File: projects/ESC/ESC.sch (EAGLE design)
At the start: 93 parts, among them J1 1755529, J2 1755529, J3 1755529, J4 1755529, U1 STM32F405RGT6, U10 CSD88584Q5DCT, U11 CSD88584Q5DCT, U12 CSD88584Q5DCT, U13 CSD88584Q5DCT, U14 SN74CBTLV3257PWR, U15 CSD88584Q5DCT, U16 CSD88584Q5DCT, U17 CSD88584Q5DCT, U2 CSD88584Q5DCT, U3 CSD88584Q5DCT, U4 CSD88584Q5DCT, U8 CSD88584Q5DCT, U9 CSD88584Q5DCT, Y1 ECS-80-S-4X

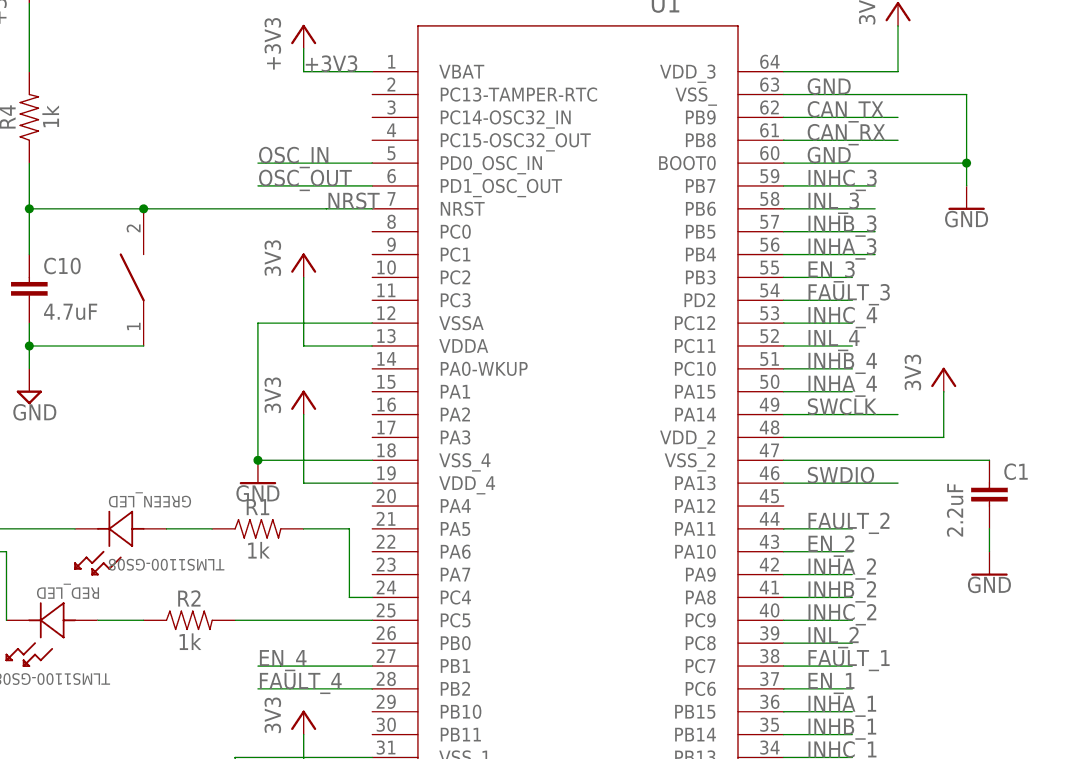
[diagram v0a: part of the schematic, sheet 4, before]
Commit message: All DRVs connected to STM
now for the fun part...
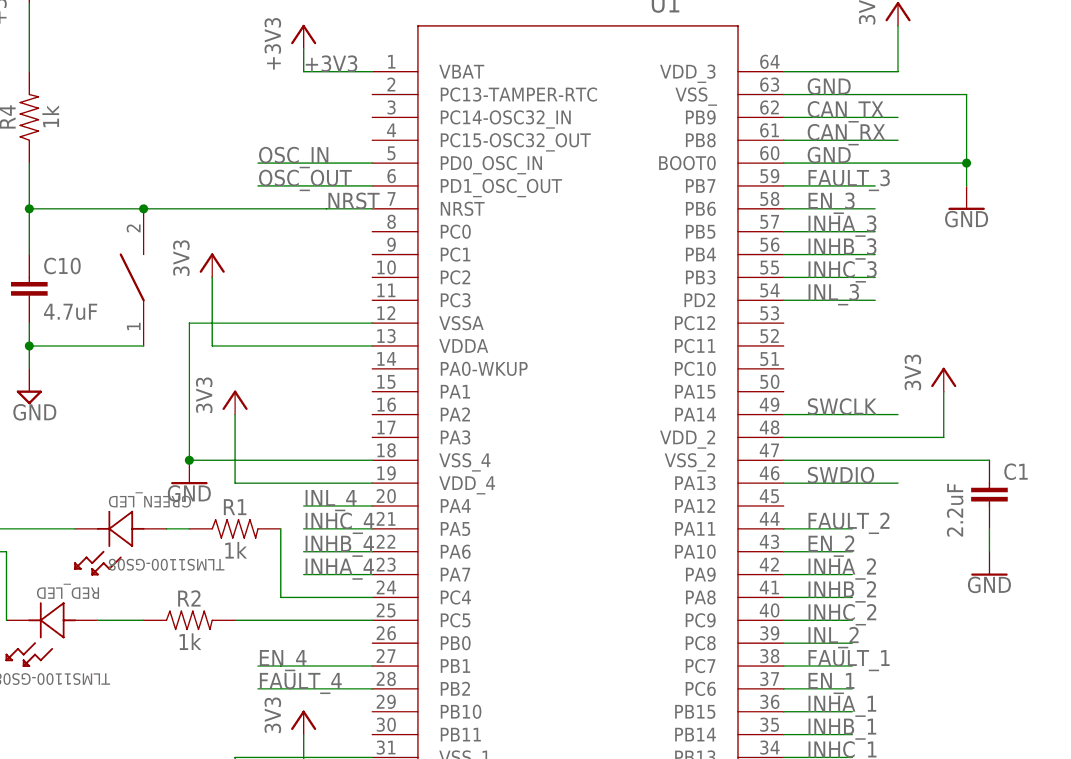
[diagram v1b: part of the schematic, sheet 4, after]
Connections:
- net EN_3: now also U1.PB6; no longer U1.PB3
- net FAULT_3: now also U1.PB7; no longer U1.PD2
- net INHA_3: now also U1.PB5; no longer U1.PB4
- net INHA_4: now also U1.PA7; no longer U1.PA15
- net INHB_3: now also U1.PB4; no longer U1.PB5
- net INHB_4: now also U1.PA6; no longer U1.PC10
- net INHC_3: now also U1.PB3; no longer U1.PB7
- net INHC_4: now also U1.PA5; no longer U1.PC12
- net INL_3: now also U1.PD2; no longer U1.PB6
- net INL_4: now also U1.PA4; no longer U1.PC11
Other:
- moved on the sheet: R1
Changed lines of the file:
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@@
 <attribute name="VALUE" x="91.1606" y="113.2586" size="2.0828" layer="96" ratio="6" rot="SR0"/>
 </instance>
-<instance part="R1" gate="G$1" x="63.5" y="53.34" smashed="yes">
-<attribute name="NAME" x="63.5" y="54.864" size="1.778" layer="95" font="vector" align="bottom-center"/>
-<attribute name="VALUE" x="63.5" y="51.816" size="1.778" layer="96" font="vector" align="top-center"/>
+<instance part="R1" gate="G$1" x="60.96" y="53.34" smashed="yes">
+<attribute name="NAME" x="60.96" y="54.864" size="1.778" layer="95" font="vector" align="bottom-center"/>
+<attribute name="VALUE" x="60.96" y="51.816" size="1.778" layer="96" font="vector" align="top-center"/>
 </instance>
 <instance part="R2" gate="G$1" x="55.88" y="43.18" smashed="yes">
@@
 <attribute name="VALUE" x="142.24" y="88.646" size="1.778" layer="96" align="top-center"/>
 </instance>
-<instance part="GND24" gate="1" x="63.5" y="58.42" smashed="yes">
-<attribute name="VALUE" x="63.5" y="58.166" size="1.778" layer="96" align="top-center"/>
-</instance>
-<instance part="3V1" gate="VCC" x="68.58" y="83.82" smashed="yes">
-<attribute name="VALUE" x="66.04" y="81.28" size="1.778" layer="96" rot="R90"/>
+<instance part="GND24" gate="1" x="55.88" y="58.42" smashed="yes">
+<attribute name="VALUE" x="55.88" y="58.166" size="1.778" layer="96" align="top-center"/>
+</instance>
+<instance part="3V1" gate="VCC" x="58.42" y="83.82" smashed="yes">
+<attribute name="VALUE" x="55.88" y="81.28" size="1.778" layer="96" rot="R90"/>
 </instance>
 <instance part="C10" gate="G$1" x="38.1" y="78.74" smashed="yes">
@@
 <attribute name="VALUE" x="137.16" y="68.58" size="1.778" layer="96" rot="R90"/>
 </instance>
-<instance part="3V6" gate="VCC" x="68.58" y="68.58" smashed="yes">
-<attribute name="VALUE" x="66.04" y="66.04" size="1.778" layer="96" rot="R90"/>
+<instance part="3V6" gate="VCC" x="60.96" y="68.58" smashed="yes">
+<attribute name="VALUE" x="58.42" y="66.04" size="1.778" layer="96" rot="R90"/>
 </instance>
 <instance part="3V7" gate="VCC" x="68.58" y="33.02" smashed="yes">
@@
 <segment>
 <pinref part="U1" gate="A" pin="PC4"/>
-<wire x1="76.2" y1="45.72" x2="73.66" y2="45.72" width="0.1524" layer="91"/>
 <pinref part="R1" gate="G$1" pin="2"/>
-<wire x1="68.58" y1="53.34" x2="73.66" y2="53.34" width="0.1524" layer="91"/>
-<wire x1="73.66" y1="53.34" x2="73.66" y2="45.72" width="0.1524" layer="91"/>
+<wire x1="66.04" y1="53.34" x2="66.04" y2="45.72" width="0.1524" layer="91"/>
+<wire x1="66.04" y1="45.72" x2="76.2" y2="45.72" width="0.1524" layer="91"/>
 </segment>
 </net>
@@
 <pinref part="R1" gate="G$1" pin="1"/>
 <pinref part="GREEN_LED" gate="A" pin="2"/>
-<wire x1="53.34" y1="53.34" x2="58.42" y2="53.34" width="0.1524" layer="91"/>
+<wire x1="53.34" y1="53.34" x2="55.88" y2="53.34" width="0.1524" layer="91"/>
 </segment>
 </net>
@@
 <pinref part="U1" gate="A" pin="VSSA"/>
 <pinref part="GND24" gate="1" pin="GND"/>
-<wire x1="76.2" y1="76.2" x2="63.5" y2="76.2" width="0.1524" layer="91"/>
-<wire x1="63.5" y1="76.2" x2="63.5" y2="60.96" width="0.1524" layer="91"/>
+<wire x1="76.2" y1="76.2" x2="55.88" y2="76.2" width="0.1524" layer="91"/>
+<wire x1="55.88" y1="76.2" x2="55.88" y2="60.96" width="0.1524" layer="91"/>
 <pinref part="U1" gate="A" pin="VSS_4"/>
-<wire x1="76.2" y1="60.96" x2="63.5" y2="60.96" width="0.1524" layer="91"/>
-<junction x="63.5" y="60.96"/>
+<wire x1="76.2" y1="60.96" x2="55.88" y2="60.96" width="0.1524" layer="91"/>
+<junction x="55.88" y="60.96"/>
 </segment>
 <segment>
@@
 </segment>
 </net>
-<net name="FAULT_3" class="0">
-<segment>
-<wire x1="121.92" y1="78.74" x2="129.54" y2="78.74" width="0.1524" layer="91"/>
-<pinref part="U1" gate="A" pin="PD2"/>
-<label x="124.46" y="78.74" size="1.778" layer="95"/>
-</segment>
-</net>
-<net name="INHA_4" class="0">
-<segment>
-<pinref part="U1" gate="A" pin="PA15"/>
-<wire x1="121.92" y1="68.58" x2="129.54" y2="68.58" width="0.1524" layer="91"/>
-<label x="124.46" y="68.58" size="1.778" layer="95"/>
-</segment>
-</net>
-<net name="INHB_4" class="0">
-<segment>
-<pinref part="U1" gate="A" pin="PC10"/>
-<wire x1="121.92" y1="71.12" x2="129.54" y2="71.12" width="0.1524" layer="91"/>
-<label x="124.46" y="71.12" size="1.778" layer="95"/>
-</segment>
-</net>
-<net name="INHC_4" class="0">
-<segment>
-<wire x1="121.92" y1="76.2" x2="129.54" y2="76.2" width="0.1524" layer="91"/>
-<pinref part="U1" gate="A" pin="PC12"/>
-<label x="124.46" y="76.2" size="1.778" layer="95"/>
-</segment>
-</net>
-<net name="INL_4" class="0">
-<segment>
-<wire x1="121.92" y1="73.66" x2="129.54" y2="73.66" width="0.1524" layer="91"/>
-<pinref part="U1" gate="A" pin="PC11"/>
-<label x="124.46" y="73.66" size="1.778" layer="95"/>
-</segment>
-</net>
 <net name="EN_4" class="0">
 <segment>
@@
 <pinref part="U1" gate="A" pin="VDDA"/>
 <pinref part="3V1" gate="VCC" pin="VCC"/>
-<wire x1="76.2" y1="73.66" x2="68.58" y2="73.66" width="0.1524" layer="91"/>
-<wire x1="68.58" y1="73.66" x2="68.58" y2="81.28" width="0.1524" layer="91"/>
+<wire x1="76.2" y1="73.66" x2="58.42" y2="73.66" width="0.1524" layer="91"/>
+<wire x1="58.42" y1="73.66" x2="58.42" y2="81.28" width="0.1524" layer="91"/>
 </segment>
 <segment>
@@
 <segment>
 <pinref part="U1" gate="A" pin="VDD_4"/>
-<wire x1="76.2" y1="58.42" x2="68.58" y2="58.42" width="0.1524" layer="91"/>
+<wire x1="76.2" y1="58.42" x2="60.96" y2="58.42" width="0.1524" layer="91"/>
 <pinref part="3V6" gate="VCC" pin="VCC"/>
-<wire x1="68.58" y1="58.42" x2="68.58" y2="66.04" width="0.1524" layer="91"/>
+<wire x1="60.96" y1="58.42" x2="60.96" y2="66.04" width="0.1524" layer="91"/>
 </segment>
 </net>
@@
 </segment>
 </net>
-<net name="INHC_3" class="0">
+<net name="INL_4" class="0">
+<segment>
+<pinref part="U1" gate="A" pin="PA4"/>
+<wire x1="76.2" y1="55.88" x2="68.58" y2="55.88" width="0.1524" layer="91"/>
+<label x="68.58" y="55.88" size="1.778" layer="95"/>
+</segment>
+</net>
+<net name="INHC_4" class="0">
+<segment>
+<pinref part="U1" gate="A" pin="PA5"/>
+<wire x1="76.2" y1="53.34" x2="68.58" y2="53.34" width="0.1524" layer="91"/>
+<label x="68.58" y="53.34" size="1.778" layer="95"/>
+</segment>
+</net>
+<net name="INHB_4" class="0">
+<segment>
+<pinref part="U1" gate="A" pin="PA6"/>
+<wire x1="76.2" y1="50.8" x2="68.58" y2="50.8" width="0.1524" layer="91"/>
+<label x="68.58" y="50.8" size="1.778" layer="95"/>
+</segment>
+</net>
+<net name="INHA_4" class="0">
+<segment>
+<pinref part="U1" gate="A" pin="PA7"/>
+<wire x1="76.2" y1="48.26" x2="68.58" y2="48.26" width="0.1524" layer="91"/>
+<label x="68.58" y="48.26" size="1.778" layer="95"/>
+</segment>
+</net>
+<net name="FAULT_3" class="0">
 <segment>
 <pinref part="U1" gate="A" pin="PB7"/>
@@
 <net name="EN_3" class="0">
 <segment>
-<wire x1="121.92" y1="81.28" x2="129.54" y2="81.28" width="0.1524" layer="91"/>
-<pinref part="U1" gate="A" pin="PB3"/>
-<label x="124.46" y="81.28" size="1.778" layer="95"/>
+<pinref part="U1" gate="A" pin="PB6"/>
+<wire x1="121.92" y1="88.9" x2="132.08" y2="88.9" width="0.1524" layer="91"/>
+<label x="124.46" y="88.9" size="1.778" layer="95"/>
 </segment>
 </net>
 <net name="INHA_3" class="0">
+<segment>
+<pinref part="U1" gate="A" pin="PB5"/>
+<wire x1="121.92" y1="86.36" x2="132.08" y2="86.36" width="0.1524" layer="91"/>
+<label x="124.46" y="86.36" size="1.778" layer="95"/>
+</segment>
+</net>
+<net name="INHB_3" class="0">
 <segment>
 <pinref part="U1" gate="A" pin="PB4"/>
@@
 </segment>
 </net>
-<net name="INHB_3" class="0">
-<segment>
-<pinref part="U1" gate="A" pin="PB5"/>
-<wire x1="121.92" y1="86.36" x2="132.08" y2="86.36" width="0.1524" layer="91"/>
-<label x="124.46" y="86.36" size="1.778" layer="95"/>
+<net name="INHC_3" class="0">
+<segment>
+<pinref part="U1" gate="A" pin="PB3"/>
+<wire x1="121.92" y1="81.28" x2="132.08" y2="81.28" width="0.1524" layer="91"/>
+<label x="124.46" y="81.28" size="1.778" layer="95"/>
 </segment>
 </net>
 <net name="INL_3" class="0">
 <segment>
-<pinref part="U1" gate="A" pin="PB6"/>
-<wire x1="121.92" y1="88.9" x2="132.08" y2="88.9" width="0.1524" layer="91"/>
-<label x="124.46" y="88.9" size="1.778" layer="95"/>
-</segment>
-</net>
+<pinref part="U1" gate="A" pin="PD2"/>
+<wire x1="121.92" y1="78.74" x2="132.08" y2="78.74" width="0.1524" layer="91"/>
+<label x="124.46" y="78.74" size="1.778" layer="95"/>
+</segment>
+</net>

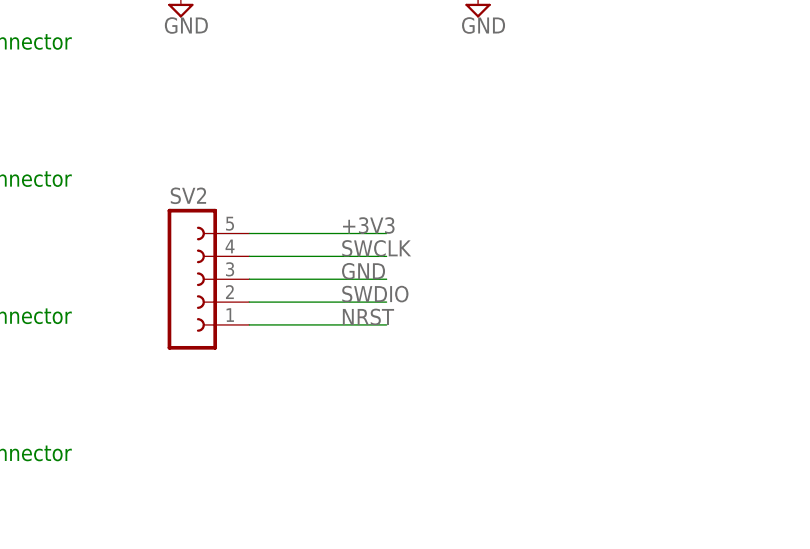
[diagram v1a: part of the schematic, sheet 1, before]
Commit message: Fixed center and schematics.
"S" on the can tranciever and "S" on the multiplexer are entirely different things. and the multiplexer distinguishes between the can module and the header pin, apparently.
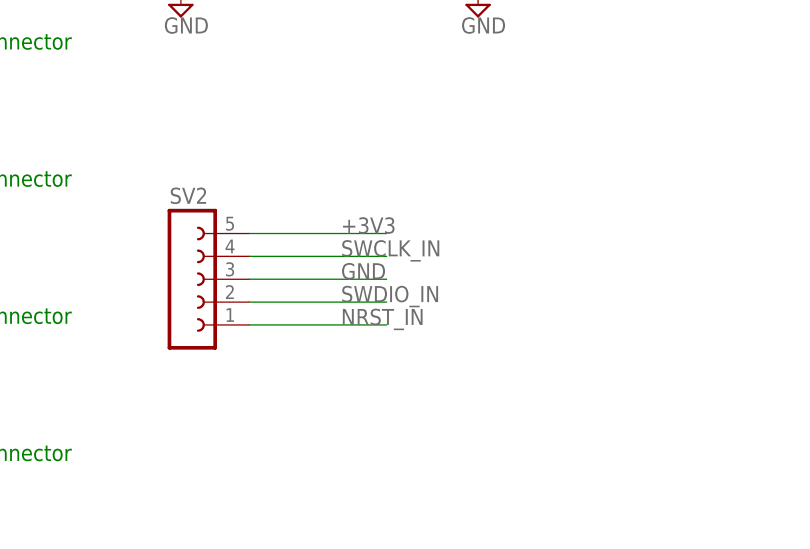
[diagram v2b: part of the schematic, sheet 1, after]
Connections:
- net NRST: no longer SV2.1
- net NRST_IN: now also SV2.1
- net S: no longer U$6.S
- net SWCLK: no longer SV2.4
- net SWCLK_IN: now also SV2.4
- net SWDIO: no longer SV2.2
- net SWDIO_IN: now also SV2.2
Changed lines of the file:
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@@
-</segment>
-</net>
-<net name="NRST" class="0">
-<segment>
-<pinref part="SV2" gate="G$1" pin="1"/>
-<wire x1="99.06" y1="38.1" x2="114.3" y2="38.1" width="0.1524" layer="91"/>
-<label x="109.22" y="38.1" size="1.778" layer="95"/>
-</segment>
-</net>
-<net name="SWDIO" class="0">
-<segment>
-<pinref part="SV2" gate="G$1" pin="2"/>
-<wire x1="99.06" y1="40.64" x2="114.3" y2="40.64" width="0.1524" layer="91"/>
-<label x="109.22" y="40.64" size="1.778" layer="95"/>
-</segment>
-</net>
-<net name="SWCLK" class="0">
-<segment>
-<pinref part="SV2" gate="G$1" pin="4"/>
-<wire x1="99.06" y1="45.72" x2="114.3" y2="45.72" width="0.1524" layer="91"/>
-<label x="109.22" y="45.72" size="1.778" layer="95"/>
 </segment>
 </net>
@@
 </segment>
 </net>
+<net name="SWCLK_IN" class="0">
+<segment>
+<pinref part="SV2" gate="G$1" pin="4"/>
+<wire x1="99.06" y1="45.72" x2="114.3" y2="45.72" width="0.1524" layer="91"/>
+<label x="109.22" y="45.72" size="1.778" layer="95"/>
+</segment>
+</net>
+<net name="SWDIO_IN" class="0">
+<segment>
+<pinref part="SV2" gate="G$1" pin="2"/>
+<wire x1="99.06" y1="40.64" x2="114.3" y2="40.64" width="0.1524" layer="91"/>
+<label x="109.22" y="40.64" size="1.778" layer="95"/>
+</segment>
+</net>
+<net name="NRST_IN" class="0">
+<segment>
+<pinref part="SV2" gate="G$1" pin="1"/>
+<wire x1="99.06" y1="38.1" x2="114.3" y2="38.1" width="0.1524" layer="91"/>
+<label x="109.22" y="38.1" size="1.778" layer="95"/>
+</segment>
+</net>
 </nets>
 </sheet>
@@
 </segment>
 </net>
-<net name="S" class="0">
-<segment>
-<pinref part="U$6" gate="G$1" pin="S"/>
-<wire x1="129.54" y1="76.2" x2="139.7" y2="76.2" width="0.1524" layer="91"/>
-<label x="137.16" y="76.2" size="1.778" layer="95"/>
-</segment>
-</net>

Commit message: Made naming changes to VM and SL to 12 and GND
Changed the names for the motor voltage sources to 12 and gnd. only thing left is to connect the 12 volt supply to the 6-packs, might need another layer.
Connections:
- removed net SLA_1: U$2G$1.SLA, U3.PGND, U3.PGND_2, U3.PGND_3, U3.PGND_4, U3.PGND_5, U3.PGND_6, U3.PGND_7, U3.PGND_8, U3.PGND_9
- removed net SLA_2: U$3G$1.SLA, U9.PGND, U9.PGND_2, U9.PGND_3, U9.PGND_4, U9.PGND_5, U9.PGND_6, U9.PGND_7, U9.PGND_8, U9.PGND_9
- removed net SLA_3: U$4G$1.SLA, U12.PGND, U12.PGND_2, U12.PGND_3, U12.PGND_4, U12.PGND_5, U12.PGND_6, U12.PGND_7, U12.PGND_8, U12.PGND_9
- removed net SLA_4: U$7G$1.SLA, U16.PGND, U16.PGND_2, U16.PGND_3, U16.PGND_4, U16.PGND_5, U16.PGND_6, U16.PGND_7, U16.PGND_8, U16.PGND_9
- removed net SLB_1: U$2G$1.SLB, U4.PGND, U4.PGND_2, U4.PGND_3, U4.PGND_4, U4.PGND_5, U4.PGND_6, U4.PGND_7, U4.PGND_8, U4.PGND_9
- removed net SLB_2: U$3G$1.SLB, U10.PGND, U10.PGND_2, U10.PGND_3, U10.PGND_4, U10.PGND_5, U10.PGND_6, U10.PGND_7, U10.PGND_8, U10.PGND_9
- removed net SLB_3: U$4G$1.SLB, U13.PGND, U13.PGND_2, U13.PGND_3, U13.PGND_4, U13.PGND_5, U13.PGND_6, U13.PGND_7, U13.PGND_8, U13.PGND_9
- removed net SLB_4: U$7G$1.SLB, U17.PGND, U17.PGND_2, U17.PGND_3, U17.PGND_4, U17.PGND_5, U17.PGND_6, U17.PGND_7, U17.PGND_8, U17.PGND_9
- removed net SLC_1: U$2G$1.SLC, U2.PGND, U2.PGND_2, U2.PGND_3, U2.PGND_4, U2.PGND_5, U2.PGND_6, U2.PGND_7, U2.PGND_8, U2.PGND_9
- removed net SLC_2: U$3G$1.SLC, U8.PGND, U8.PGND_2, U8.PGND_3, U8.PGND_4, U8.PGND_5, U8.PGND_6, U8.PGND_7, U8.PGND_8, U8.PGND_9
- removed net SLC_3: U$4G$1.SLC, U11.PGND, U11.PGND_2, U11.PGND_3, U11.PGND_4, U11.PGND_5, U11.PGND_6, U11.PGND_7, U11.PGND_8, U11.PGND_9
- removed net SLC_4: U$7G$1.SLC, U15.PGND, U15.PGND_2, U15.PGND_3, U15.PGND_4, U15.PGND_5, U15.PGND_6, U15.PGND_7, U15.PGND_8, U15.PGND_9
- removed net VM_1: C15.1, C17.2, U$2G$1.VDRAIN, U$2G$2.VM, U2.VIN, U3.VIN, U4.VIN
- removed net VM_2: C21.1, C22.2, U$3G$1.VDRAIN, U$3G$2.VM, U10.VIN, U8.VIN, U9.VIN
- removed net VM_3: C25.1, C26.2, U$4G$1.VDRAIN, U$4G$2.VM, U11.VIN, U12.VIN, U13.VIN
- removed net VM_4: C29.1, C36.2, U$7G$1.VDRAIN, U$7G$2.VM, U15.VIN, U16.VIN, U17.VIN
- net +12V: now also C15.1, C17.2, C21.1, C22.2, C25.1, C26.2, C29.1, C36.2, U$2G$1.VDRAIN, U$2G$2.VM, U$3G$1.VDRAIN, U$3G$2.VM, U$4G$1.VDRAIN, U$4G$2.VM, U$7G$1.VDRAIN, U$7G$2.VM, U10.VIN, U11.VIN, U12.VIN, U13.VIN, U15.VIN, U16.VIN, U17.VIN, U2.VIN, U3.VIN, U4.VIN, U8.VIN, U9.VIN
- net GND: now also U$2G$1.SLA, U$2G$1.SLB, U$2G$1.SLC, U$3G$1.SLA, U$3G$1.SLB, U$3G$1.SLC, U$4G$1.SLA, U$4G$1.SLB, U$4G$1.SLC, U$7G$1.SLA, U$7G$1.SLB, U$7G$1.SLC, U10.PGND, U10.PGND_2, U10.PGND_3, U10.PGND_4, U10.PGND_5, U10.PGND_6, U10.PGND_7, U10.PGND_8, U10.PGND_9, U11.PGND, U11.PGND_2, U11.PGND_3, U11.PGND_4, U11.PGND_5, U11.PGND_6, U11.PGND_7, U11.PGND_8, U11.PGND_9, U12.PGND, U12.PGND_2, U12.PGND_3, U12.PGND_4, U12.PGND_5, U12.PGND_6, U12.PGND_7, U12.PGND_8, U12.PGND_9, U13.PGND, U13.PGND_2, U13.PGND_3, U13.PGND_4, U13.PGND_5, U13.PGND_6, U13.PGND_7, U13.PGND_8, U13.PGND_9, U15.PGND, U15.PGND_2, U15.PGND_3, U15.PGND_4, U15.PGND_5, U15.PGND_6, U15.PGND_7, U15.PGND_8, U15.PGND_9, U16.PGND, U16.PGND_2, U16.PGND_3, U16.PGND_4, U16.PGND_5, U16.PGND_6, U16.PGND_7, U16.PGND_8, U16.PGND_9, U17.PGND, U17.PGND_2, U17.PGND_3, U17.PGND_4, U17.PGND_5, U17.PGND_6, U17.PGND_7, U17.PGND_8, U17.PGND_9, U2.PGND, U2.PGND_2, U2.PGND_3, U2.PGND_4, U2.PGND_5, U2.PGND_6, U2.PGND_7, U2.PGND_8, U2.PGND_9, U3.PGND, U3.PGND_2, U3.PGND_3, U3.PGND_4, U3.PGND_5, U3.PGND_6, U3.PGND_7, U3.PGND_8, U3.PGND_9, U4.PGND, U4.PGND_2, U4.PGND_3, U4.PGND_4, U4.PGND_5, U4.PGND_6, U4.PGND_7, U4.PGND_8, U4.PGND_9, U8.PGND, U8.PGND_2, U8.PGND_3, U8.PGND_4, U8.PGND_5, U8.PGND_6, U8.PGND_7, U8.PGND_8, U8.PGND_9, U9.PGND, U9.PGND_2, U9.PGND_3, U9.PGND_4, U9.PGND_5, U9.PGND_6, U9.PGND_7, U9.PGND_8, U9.PGND_9
